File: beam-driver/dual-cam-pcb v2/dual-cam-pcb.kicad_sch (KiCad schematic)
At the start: 48 parts, among them J1 Conn_01x08_Pin, J2 Conn_01x08_Pin, J3 Conn_Coaxial, J4 LED connector, J5 LED connector, J6 tilt, J7 pan, J8 Conn_XT_Sink, Q1 Q_NMOS_GDS, U1 Pico, U2 PUCC27624DR, U3 LM317L_SOT-89, U4 LM7805_TO220

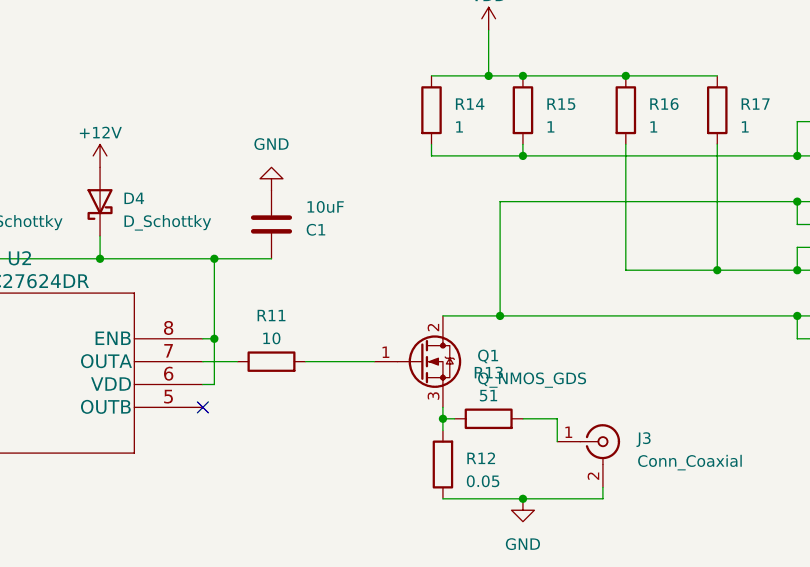
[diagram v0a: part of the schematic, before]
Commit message: update dual-cam-pcb
* change some footprints
* add miller capacitor (to smooth out led transitions)
* add pcb name
* minor layout changes
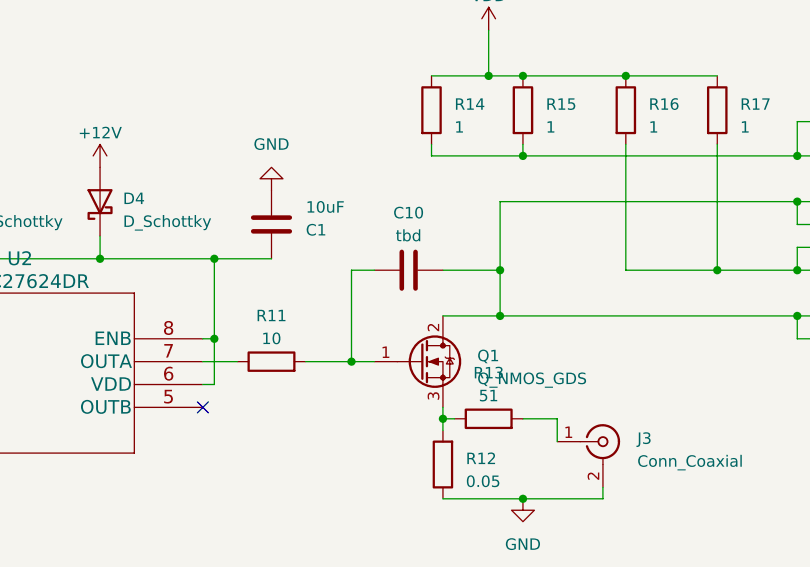
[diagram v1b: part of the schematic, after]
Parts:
- added C10: tbd, Capacitor_SMD:C_0603_1608Metric_Pad1.08x0.95mm_HandSolder, symbol Device:C
- C7: footprint Capacitor_SMD:C_0805_2012Metric_Pad1.18x1.45mm_HandSolder -> Capacitor_SMD:C_1206_3216Metric_Pad1.33x1.80mm_HandSolder
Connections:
- net at Q1.1 (G), R11.2: now also C10.2
- net at J4.5 (minus1), J4.6 (minus2), J5.5 (minus1)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: now also C10.1
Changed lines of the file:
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@@
   (junction (at 111.76 66.04) (diameter 0) (color 0 0 0 0)
   )
+  (junction (at 212.09 44.45) (diameter 0) (color 0 0 0 0)
+  )
   (junction (at 34.29 152.4) (diameter 0) (color 0 0 0 0)
   )
@@
   )
   (junction (at 245.11 31.75) (diameter 0) (color 0 0 0 0)
+  )
+  (junction (at 195.58 54.61) (diameter 0) (color 0 0 0 0)
   )
   (junction (at 245.11 44.45) (diameter 0) (color 0 0 0 0)
@@
     (stroke (width 0) (type default))
   )
-  (wire (pts (xy 190.5 54.61) (xy 198.12 54.61))
+  (wire (pts (xy 190.5 54.61) (xy 195.58 54.61))
     (stroke (width 0) (type default))
   )
@@
     (stroke (width 0) (type default))
   )
+  (wire (pts (xy 195.58 54.61) (xy 198.12 54.61))
+    (stroke (width 0) (type default))
+  )
   (wire (pts (xy 66.04 50.8) (xy 66.04 80.01))
     (stroke (width 0) (type default))
@@
     (stroke (width 0) (type default))
   )
+  (wire (pts (xy 195.58 44.45) (xy 195.58 54.61))
+    (stroke (width 0) (type default))
+  )
   (wire (pts (xy 45.72 123.19) (xy 45.72 124.46))
     (stroke (width 0) (type default))
@@
     (stroke (width 0) (type default))
   )
+  (wire (pts (xy 205.74 44.45) (xy 212.09 44.45))
+    (stroke (width 0) (type default))
+  )
   (wire (pts (xy 109.22 40.64) (xy 111.76 40.64))
     (stroke (width 0) (type default))
@@
     (stroke (width 0) (type default))
   )
+  (wire (pts (xy 212.09 44.45) (xy 212.09 49.53))
+    (stroke (width 0) (type default))
+  )
   (wire (pts (xy 27.94 153.67) (xy 31.75 153.67))
     (stroke (width 0) (type default))
@@
     (stroke (width 0) (type default))
   )
+  (wire (pts (xy 198.12 44.45) (xy 195.58 44.45))
+    (stroke (width 0) (type default))
+  )
   (wire (pts (xy 257.81 27.94) (xy 245.11 27.94))
     (stroke (width 0) (type default))
@@
     (stroke (width 0) (type default))
   )
-  (wire (pts (xy 212.09 36.83) (xy 212.09 49.53))
+  (wire (pts (xy 212.09 36.83) (xy 212.09 44.45))
     (stroke (width 0) (type default))
   )
@@
         (path "/f2fe1216-cc57-4cd7-9f23-2fb3f137cc5f"
           (reference "U4") (unit 1)
+        )
+      )
+    )
+  )
+  (symbol (lib_id "Device:C") (at 201.93 44.45 270) (mirror x) (unit 1)
+    (in_bom yes) (on_board yes) (dnp no) (fields_autoplaced)
+    (property "Reference" "C10" (at 201.93 38.1 90)
+      (effects (font (size 1.27 1.27)))
+    )
+    (property "Value" "tbd" (at 201.93 40.64 90)
+      (effects (font (size 1.27 1.27)))
+    )
+    (property "Footprint" "Capacitor_SMD:C_0603_1608Metric_Pad1.08x0.95mm_HandSolder" (at 198.12 43.4848 0)
+      (effects (font (size 1.27 1.27)) hide)
+    )
+    (property "Datasheet" "~" (at 201.93 44.45 0)
+      (effects (font (size 1.27 1.27)) hide)
+    )
+    (pin "1")
+    (pin "2")
+    (instances
+      (project "dual-cam-pcb"
+        (path "/f2fe1216-cc57-4cd7-9f23-2fb3f137cc5f"
+          (reference "C10") (unit 1)
         )
       )
@@
       (effects (font (size 1.27 1.27)) (justify right))
     )
-    (property "Footprint" "Capacitor_SMD:C_0805_2012Metric_Pad1.18x1.45mm_HandSolder" (at 96.2152 118.11 0)
-      (effects (font (size 1.27 1.27)) hide)
-    )
+    (property "Footprint" "Capacitor_SMD:C_1206_3216Metric_Pad1.33x1.80mm_HandSolder" (at 96.2152 118.11 0)
+      (effects (font (size 1.27 1.27)) hide)
+    )
